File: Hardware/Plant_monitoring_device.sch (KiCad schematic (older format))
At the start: 67 parts, among them J1 Barrel_Jack, J10 NXW-02, J11 NXW-03, J12 NXW-03, J13 NXW-03, J14 NXW-03, J2 SWO, J3 NXW-02, J4 NXW-02, J5 NXW-02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

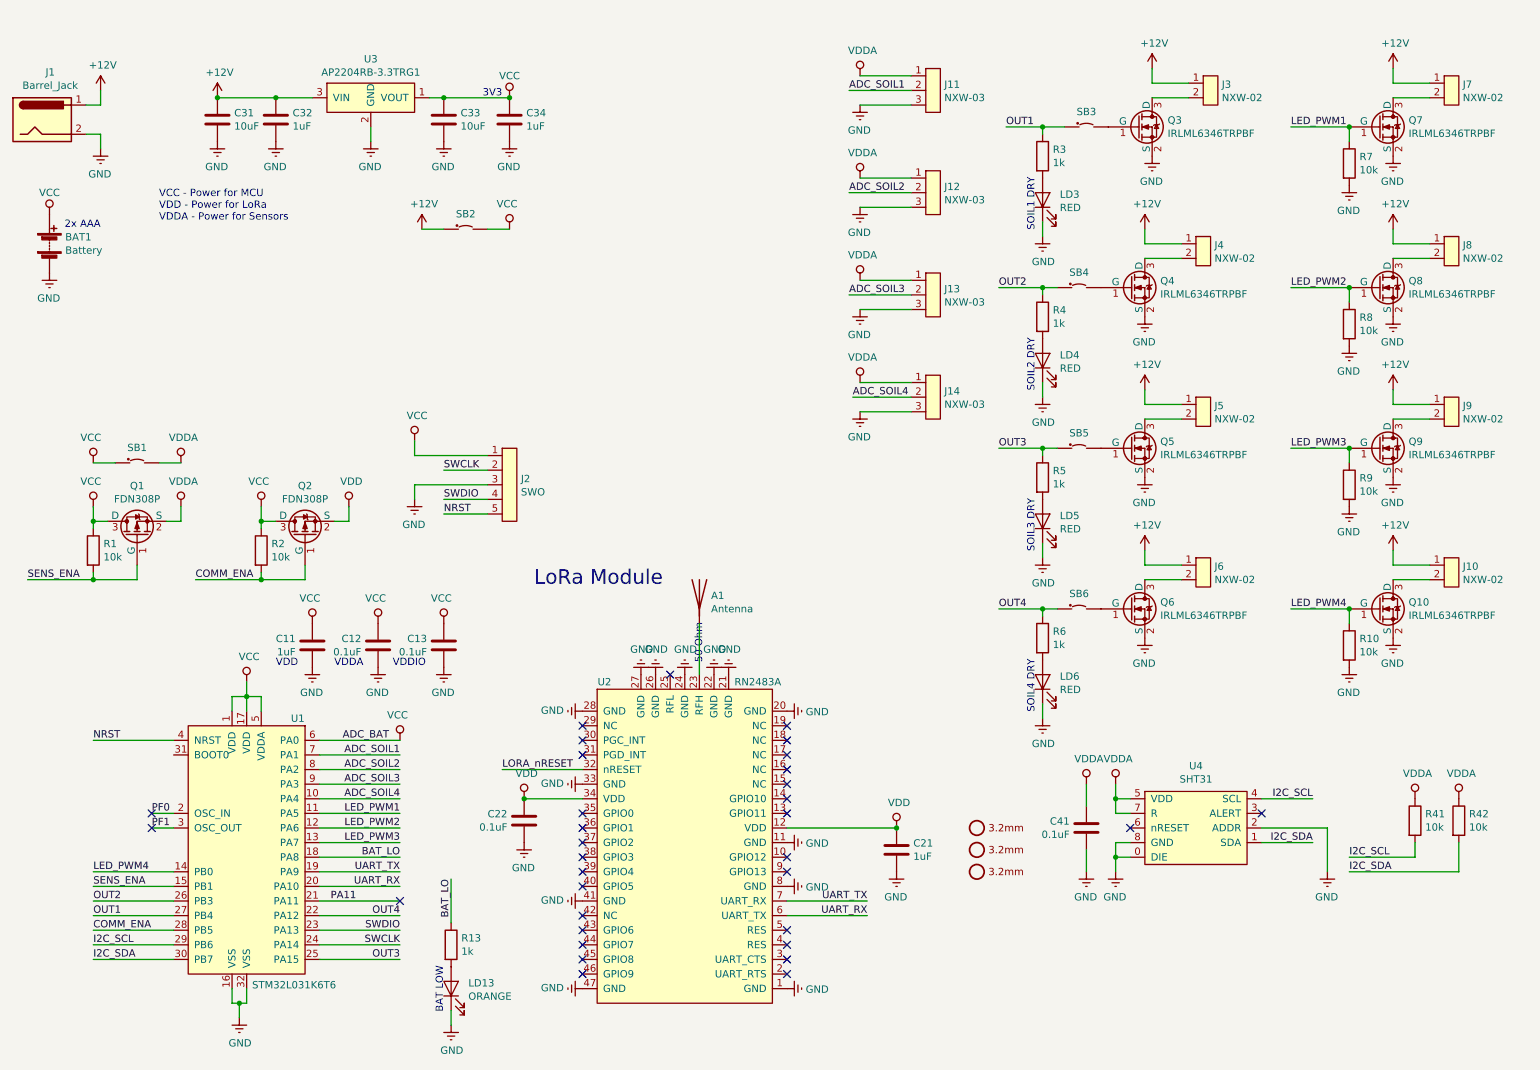
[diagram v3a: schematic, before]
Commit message: Added missing TME Symbols. Generated BOM.
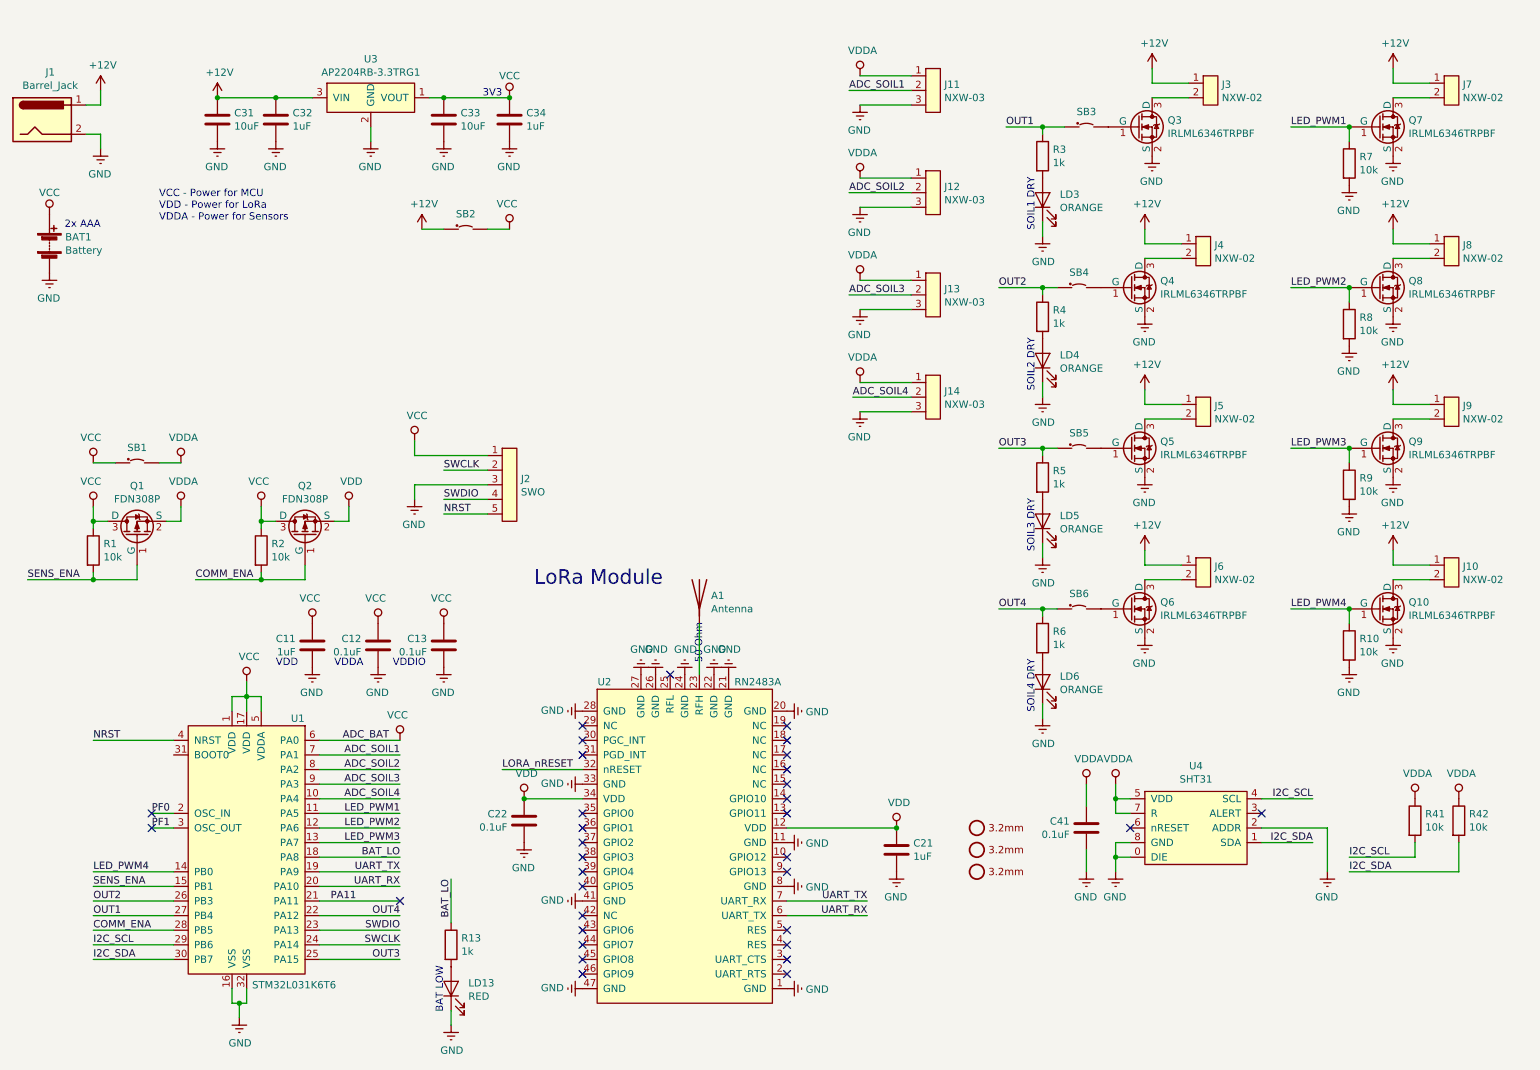
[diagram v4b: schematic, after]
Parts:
- C11, C21, C32, C34: TME (none) -> CL10A105KA8NNNC
- C12, C13, C22, C41: TME (none) -> CL10B104KO8NNNC
- C31, C33: TME (none) -> CL10A106MO8NQNC
- LD13: value ORANGE -> RED; TME (none) -> LTST-C170KRKT
- LD3, LD4, LD5, LD6: value RED -> ORANGE; TME (none) -> LTST-C170KFKT
- R1, R10, R2, R41, R42, R7, R8, R9: TME (none) -> WF06P-10K-5%
- R13, R3, R4, R5, R6: TME (none) -> WF06P-1K-5%
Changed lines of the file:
@@
 P 7750 1650
 F 0 "LD3" V 7788 1532 50  0000 R CNN
-F 1 "RED" V 7697 1532 50  0000 R CNN
+F 1 "ORANGE" V 7697 1532 50  0000 R CNN
 F 2 "MRS_Diodes:LED_0805" H 7750 1400 50  0001 C CNN
 F 3 "" H 7750 1750 50  0001 C CNN
+F 4 "LTST-C170KFKT" V 7750 1650 50  0001 C CNN "TME"
 	1    7750 1650
 	0    -1   -1   0
@@
 P 7750 2750
 F 0 "LD4" V 7788 2632 50  0000 R CNN
-F 1 "RED" V 7697 2632 50  0000 R CNN
+F 1 "ORANGE" V 7697 2632 50  0000 R CNN
 F 2 "MRS_Diodes:LED_0805" H 7750 2500 50  0001 C CNN
 F 3 "" H 7750 2850 50  0001 C CNN
+F 4 "LTST-C170KFKT" V 7750 2750 50  0001 C CNN "TME"
 	1    7750 2750
 	0    -1   -1   0
@@
 P 7750 3850
 F 0 "LD5" V 7788 3732 50  0000 R CNN
-F 1 "RED" V 7697 3732 50  0000 R CNN
+F 1 "ORANGE" V 7697 3732 50  0000 R CNN
 F 2 "MRS_Diodes:LED_0805" H 7750 3600 50  0001 C CNN
 F 3 "" H 7750 3950 50  0001 C CNN
+F 4 "LTST-C170KFKT" V 7750 3850 50  0001 C CNN "TME"
 	1    7750 3850
 	0    -1   -1   0
@@
 P 7750 4950
 F 0 "LD6" V 7788 4832 50  0000 R CNN
-F 1 "RED" V 7697 4832 50  0000 R CNN
+F 1 "ORANGE" V 7697 4832 50  0000 R CNN
 F 2 "MRS_Diodes:LED_0805" H 7750 4700 50  0001 C CNN
 F 3 "" H 7750 5050 50  0001 C CNN
+F 4 "LTST-C170KFKT" V 7750 4950 50  0001 C CNN "TME"
 	1    7750 4950
 	0    -1   -1   0
@@
 P 3700 7050
 F 0 "LD13" V 3738 6932 50  0000 R CNN
-F 1 "ORANGE" V 3647 6932 50  0000 R CNN
+F 1 "RED" V 3647 6932 50  0000 R CNN
 F 2 "MRS_Diodes:LED_0805" H 3700 6800 50  0001 C CNN
 F 3 "" H 3700 7150 50  0001 C CNN
+F 4 "LTST-C170KRKT" V 3700 7050 50  0001 C CNN "TME"
 	1    3700 7050
 	0    -1   -1   0
@@
 F 2 "MRS_Passives:R0603" V 8150 1350 50  0001 C CNN
 F 3 "" V 7830 1350 50  0001 C CNN
+F 4 "WF06P-1K-5%" H 7750 1350 50  0001 C CNN "TME"
 	1    7750 1350
 	1    0    0    -1
@@
 F 2 "MRS_Passives:R0603" V 8150 2450 50  0001 C CNN
 F 3 "" V 7830 2450 50  0001 C CNN
+F 4 "WF06P-1K-5%" H 7750 2450 50  0001 C CNN "TME"
 	1    7750 2450
 	1    0    0    -1
@@
 F 2 "MRS_Passives:R0603" V 8150 3550 50  0001 C CNN
 F 3 "" V 7830 3550 50  0001 C CNN
+F 4 "WF06P-1K-5%" H 7750 3550 50  0001 C CNN "TME"
 	1    7750 3550
 	1    0    0    -1
@@
 F 2 "MRS_Passives:R0603" V 8150 4650 50  0001 C CNN
 F 3 "" V 7830 4650 50  0001 C CNN
+F 4 "WF06P-1K-5%" H 7750 4650 50  0001 C CNN "TME"
 	1    7750 4650
 	1    0    0    -1
@@
 F 2 "MRS_Passives:R0603" V 4100 6750 50  0001 C CNN
 F 3 "" V 3780 6750 50  0001 C CNN
+F 4 "WF06P-1K-5%" H 3700 6750 50  0001 C CNN "TME"
 	1    3700 6750
 	1    0    0    -1
@@
 F 2 "MRS_Passives:C0603" H 2750 4200 50  0001 C CNN
 F 3 "" H 2775 4800 50  0001 C CNN
+F 4 "CL10A105KA8NNNC" H 2750 4700 50  0001 C CNN "TME"
 	1    2750 4700
 	-1   0    0    -1
@@
 F 2 "MRS_Passives:C0603" H 3200 4200 50  0001 C CNN
 F 3 "" H 3225 4800 50  0001 C CNN
+F 4 "CL10B104KO8NNNC" H 3200 4700 50  0001 C CNN "TME"
 	1    3200 4700
 	-1   0    0    -1
@@
 F 2 "MRS_Passives:C0603" H 3650 4200 50  0001 C CNN
 F 3 "" H 3675 4800 50  0001 C CNN
+F 4 "CL10B104KO8NNNC" H 3650 4700 50  0001 C CNN "TME"
 	1    3650 4700
 	-1   0    0    -1
@@
 F 2 "MRS_Passives:R0603" V 11000 5900 50  0001 C CNN
 F 3 "" V 10680 5900 50  0001 C CNN
+F 4 "WF06P-10K-5%" H 10600 5900 50  0001 C CNN "TME"
 	1    10600 5900
 	1    0    0    -1
@@
 F 2 "MRS_Passives:R0603" V 10700 5900 50  0001 C CNN
 F 3 "" V 10380 5900 50  0001 C CNN
+F 4 "WF06P-10K-5%" H 10300 5900 50  0001 C CNN "TME"
 	1    10300 5900
 	1    0    0    -1
@@
 F 2 "MRS_Passives:C0603" H 2500 600 50  0001 C CNN
 F 3 "" H 2525 1200 50  0001 C CNN
+F 4 "CL10A105KA8NNNC" H 2500 1100 50  0001 C CNN "TME"
 	1    2500 1100
 	1    0    0    -1
@@
 F 2 "MRS_Passives:C0603" H 2100 600 50  0001 C CNN
 F 3 "" H 2125 1200 50  0001 C CNN
+F 4 "CL10A106MO8NQNC" H 2100 1100 50  0001 C CNN "TME"
 	1    2100 1100
 	1    0    0    -1
@@
 F 2 "MRS_Passives:C0603" H 6750 5600 50  0001 C CNN
 F 3 "" H 6775 6200 50  0001 C CNN
+F 4 "CL10A105KA8NNNC" H 6750 6100 50  0001 C CNN "TME"
 	1    6750 6100
 	1    0    0    -1
@@
 F 2 "MRS_Passives:C0603" H 4200 5400 50  0001 C CNN
 F 3 "" H 4225 6000 50  0001 C CNN
+F 4 "CL10B104KO8NNNC" H 4200 5900 50  0001 C CNN "TME"
 	1    4200 5900
 	-1   0    0    -1
@@
 F 2 "MRS_Passives:R0603" V 1650 4050 50  0001 C CNN
 F 3 "" V 1330 4050 50  0001 C CNN
+F 4 "WF06P-10K-5%" H 1250 4050 50  0001 C CNN "TME"
 	1    1250 4050
 	1    0    0    -1
@@
 F 2 "MRS_Passives:R0603" V 10250 1400 50  0001 C CNN
 F 3 "" V 9930 1400 50  0001 C CNN
+F 4 "WF06P-10K-5%" H 9850 1400 50  0001 C CNN "TME"
 	1    9850 1400
 	1    0    0    -1
@@
 F 2 "MRS_Passives:R0603" V 10250 2500 50  0001 C CNN
 F 3 "" V 9930 2500 50  0001 C CNN
+F 4 "WF06P-10K-5%" H 9850 2500 50  0001 C CNN "TME"
 	1    9850 2500
 	1    0    0    -1
@@
 F 2 "MRS_Passives:R0603" V 10250 3600 50  0001 C CNN
 F 3 "" V 9930 3600 50  0001 C CNN
+F 4 "WF06P-10K-5%" H 9850 3600 50  0001 C CNN "TME"
 	1    9850 3600
 	1    0    0    -1
@@
 F 2 "MRS_Passives:R0603" V 10250 4700 50  0001 C CNN
 F 3 "" V 9930 4700 50  0001 C CNN
+F 4 "WF06P-10K-5%" H 9850 4700 50  0001 C CNN "TME"
 	1    9850 4700
 	1    0    0    -1
@@
 F 2 "MRS_Passives:R0603" V 2800 4050 50  0001 C CNN
 F 3 "" V 2480 4050 50  0001 C CNN
+F 4 "WF06P-10K-5%" H 2400 4050 50  0001 C CNN "TME"
 	1    2400 4050
 	1    0    0    -1
@@
 F 2 "MRS_Passives:C0603" H 8050 5450 50  0001 C CNN
 F 3 "" H 8075 6050 50  0001 C CNN
+F 4 "CL10B104KO8NNNC" H 8050 5950 50  0001 C CNN "TME"
 	1    8050 5950
 	-1   0    0    -1
@@
 F 2 "MRS_Passives:C0603" H 3650 600 50  0001 C CNN
 F 3 "" H 3675 1200 50  0001 C CNN
+F 4 "CL10A106MO8NQNC" H 3650 1100 50  0001 C CNN "TME"
 	1    3650 1100
 	1    0    0    -1
@@
 F 2 "MRS_Passives:C0603" H 4100 600 50  0001 C CNN
 F 3 "" H 4125 1200 50  0001 C CNN
+F 4 "CL10A105KA8NNNC" H 4100 1100 50  0001 C CNN "TME"
 	1    4100 1100
 	1    0    0    -1

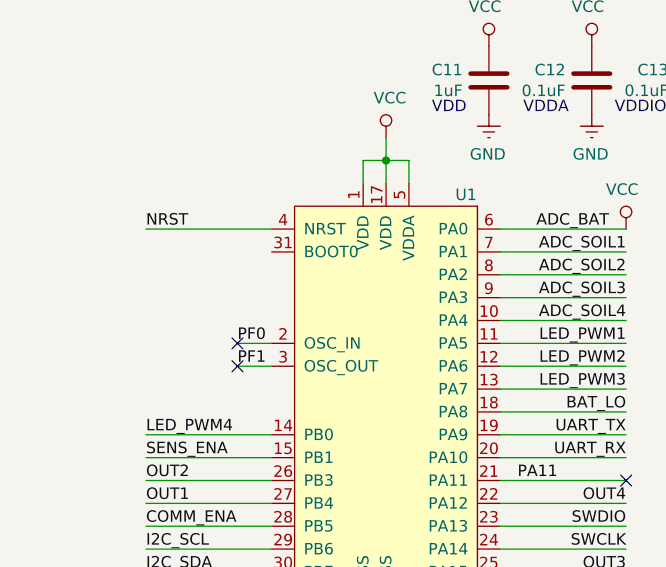
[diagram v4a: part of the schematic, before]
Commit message: Connected BOOT0 pin with GND.
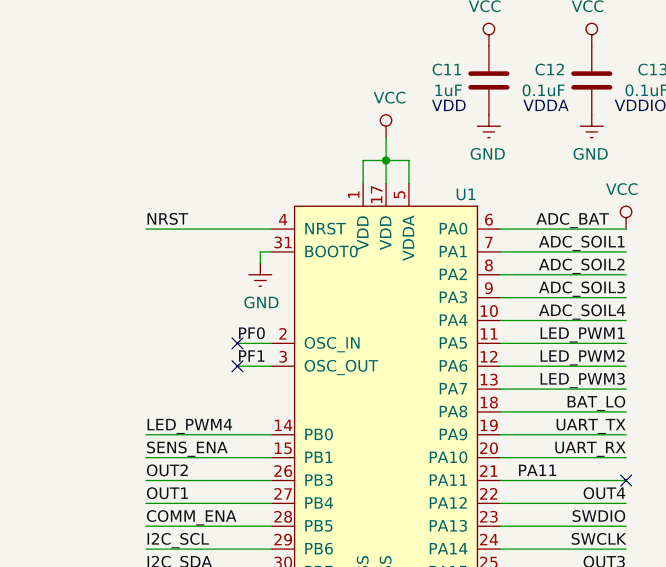
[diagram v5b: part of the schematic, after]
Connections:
- net GND: now also U1.31 (BOOT0)
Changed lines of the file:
@@
 	-1   0    0    -1
 $EndComp
+$Comp
+L MRS_Power:GND #PWR?
+U 1 1 5CDAEFB6
+P 1750 5500
+F 0 "#PWR?" H 1750 5250 50  0001 C CNN
+F 1 "GND" H 1755 5327 50  0000 C CNN
+F 2 "" H 1750 5500 50  0001 C CNN
+F 3 "" H 1750 5500 50  0001 C CNN
+	1    1750 5500
+	1    0    0    -1
+$EndComp
+Wire Wire Line
+	1750 5500 1750 5450
+Wire Wire Line
+	1750 5450 1800 5450
 $EndSCHEMATC
